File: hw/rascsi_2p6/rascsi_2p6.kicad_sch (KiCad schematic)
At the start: 88 parts, among them IC1 SN74F245DWR, IC2 SN74F245DWR, IC3 SN74F245DWR, IC4 SN74F245DWR, J1 Raspberry_Pi_2_3, J2 DNP, J4 I2C Pinout, J5 DNP, J6 CONNFLY DB-25, X1 Mac, X2 Dogcow, X3 Mac, X4 Dogcow, X5 Dogcow, X6 Dogcow, X7 Pi, X8 Pi

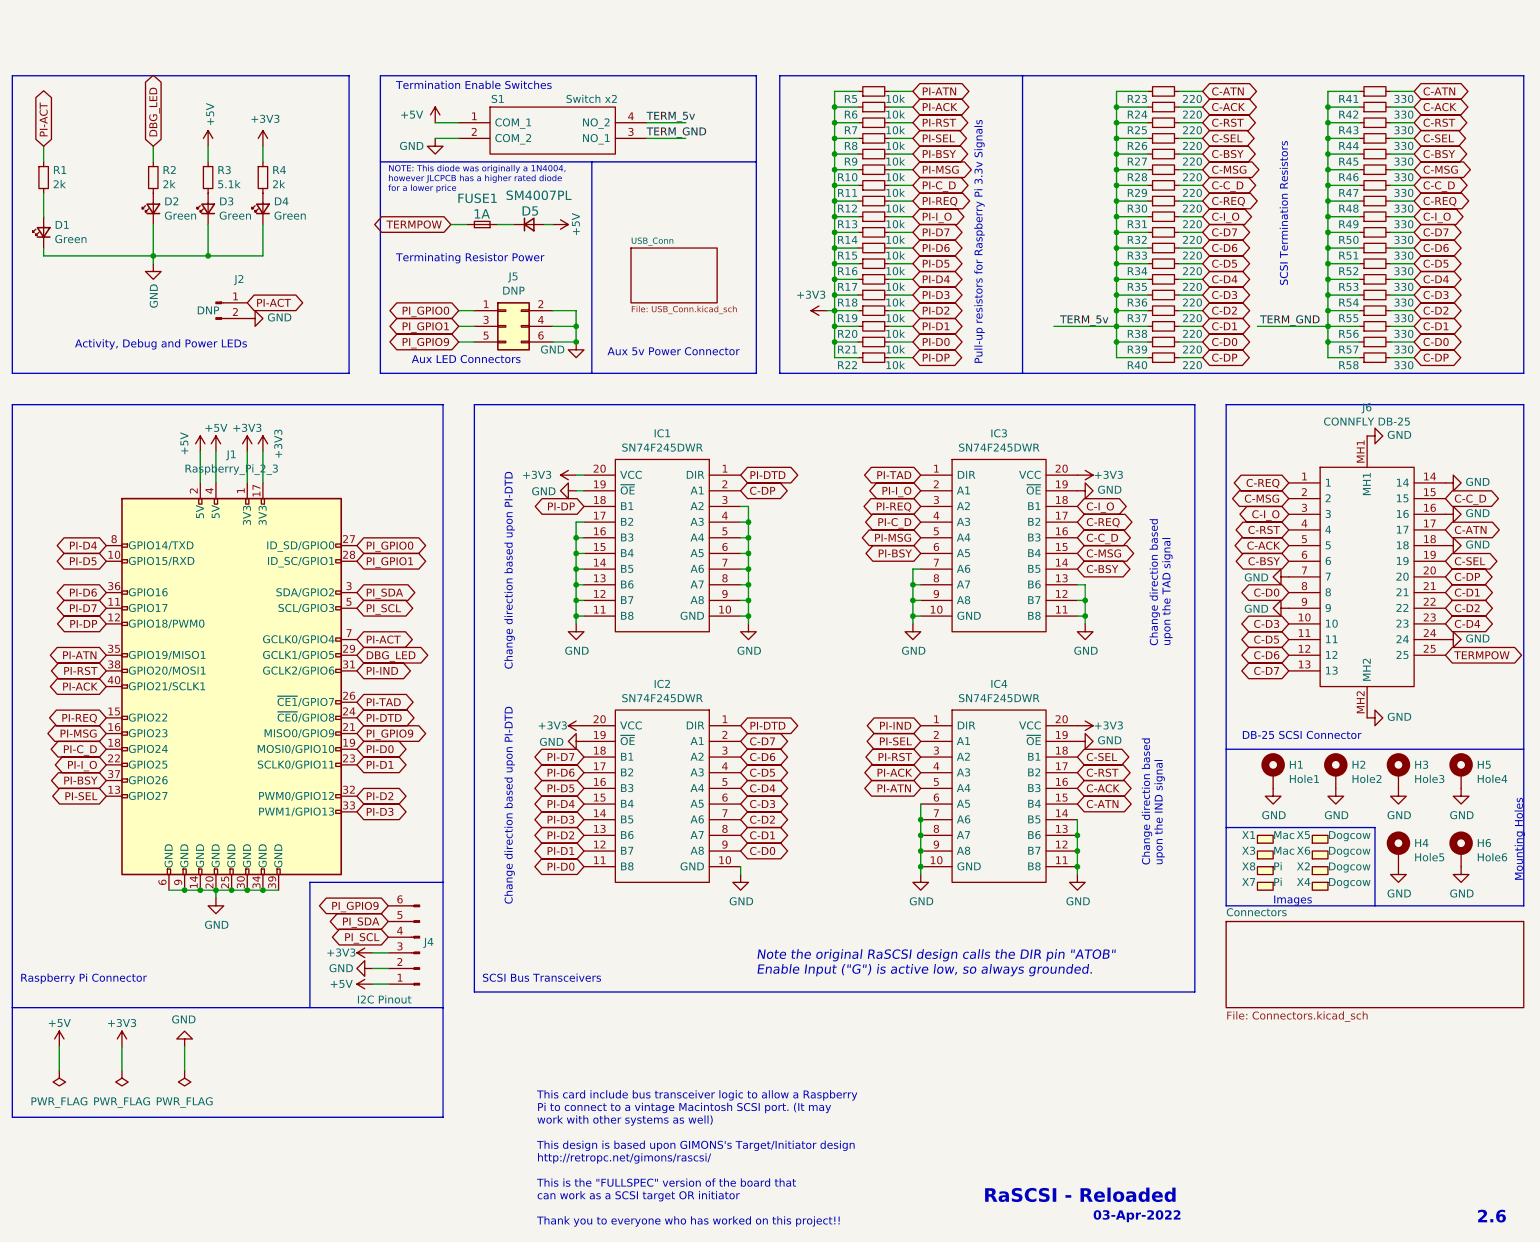
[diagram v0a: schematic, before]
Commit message: Updated with 74LVT245 - as ordered
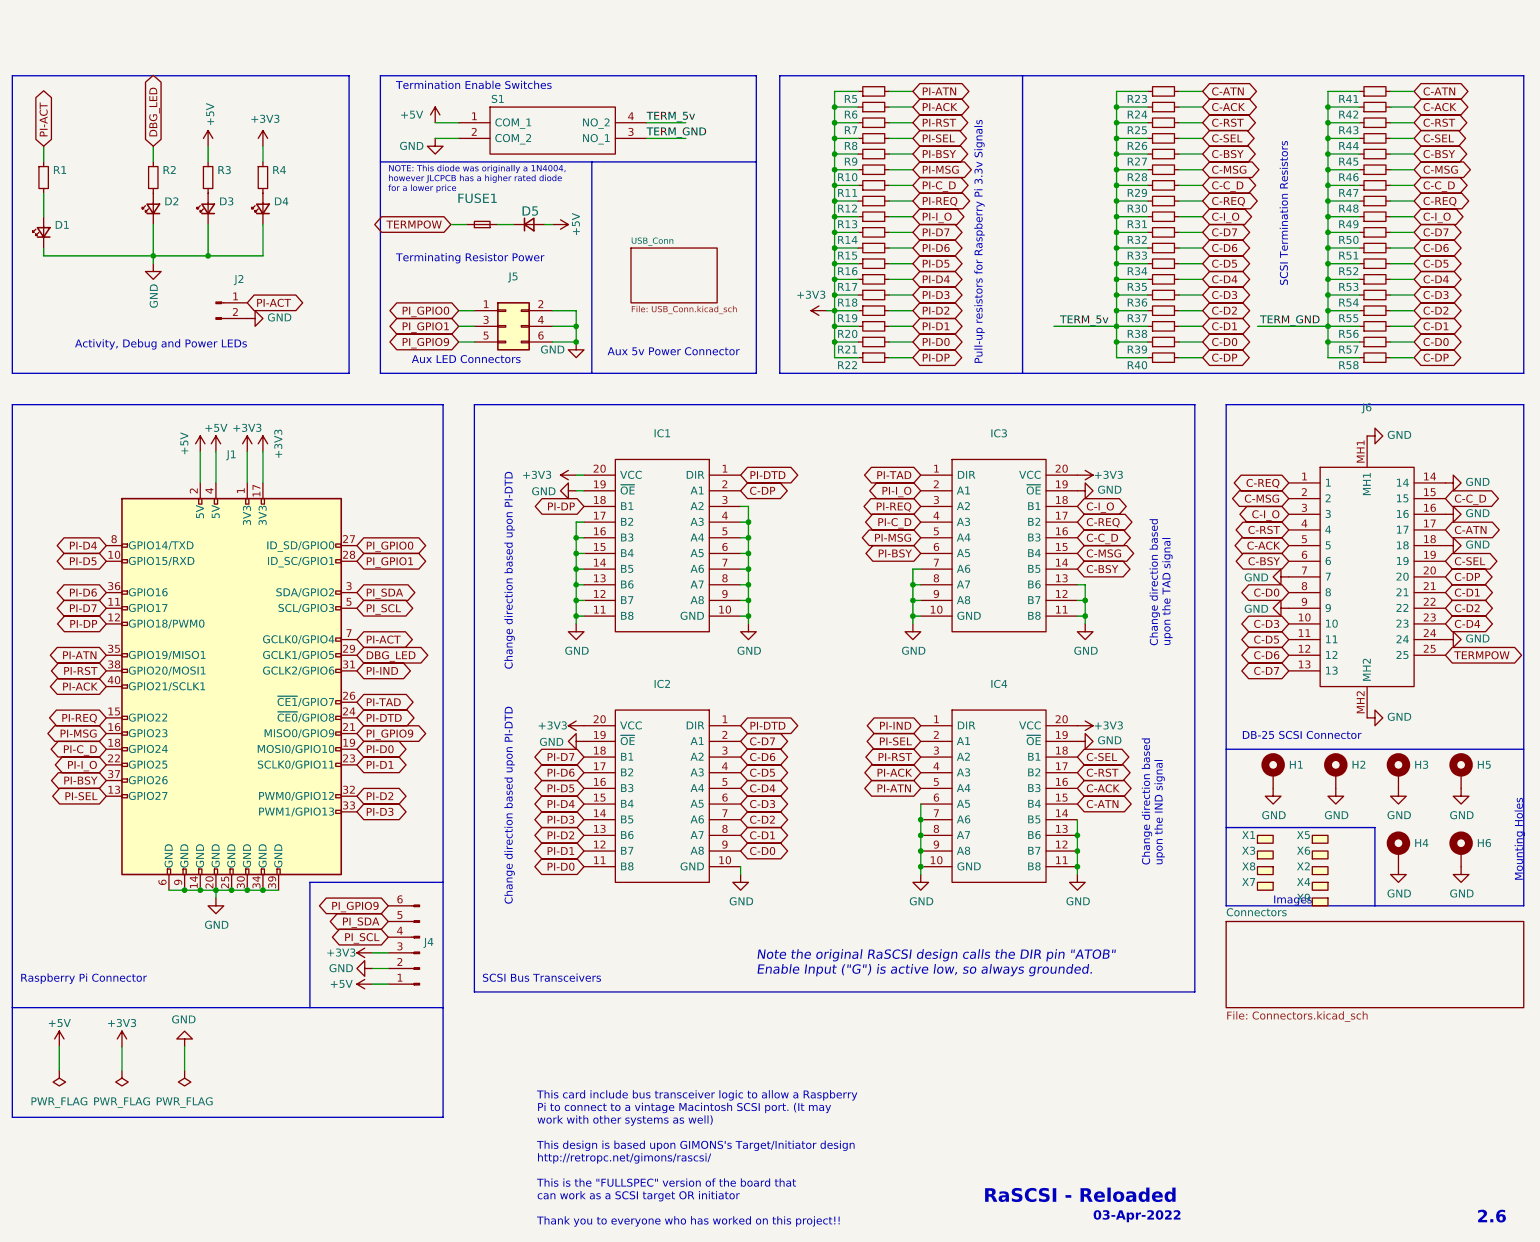
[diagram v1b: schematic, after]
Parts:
- added X9: (no value), symbol SamacSys_Parts:Logo
- D1, D2, D3, D4: value Green -> (none); footprint LED_SMD:LED_0805_2012Metric -> (none)
- D5: value SM4007PL -> (none); footprint Diode_SMD:D_SOD-123F -> (none)
- FUSE1: value 1A -> (none); footprint Fuse:Fuse_1206_3216Metric -> (none)
- H1: value Hole1 -> (none); footprint MountingHole:MountingHole_2.7mm_M2.5_Pad_Via -> (none)
- H2: value Hole2 -> (none); footprint MountingHole:MountingHole_2.7mm_M2.5_Pad_Via -> (none)
- H3: value Hole3 -> (none); footprint MountingHole:MountingHole_2.7mm_M2.5_Pad_Via -> (none)
- H4: value Hole5 -> (none); footprint MountingHole:MountingHole_2.7mm_M2.5_Pad_Via -> (none)
- H5: value Hole4 -> (none); footprint MountingHole:MountingHole_2.7mm_M2.5_Pad_Via -> (none)
- H6: value Hole6 -> (none); footprint MountingHole:MountingHole_2.7mm_M2.5_Pad_Via -> (none)
- IC1, IC2, IC3, IC4: value SN74F245DWR -> (none); footprint SamacSys_Parts:SOIC127P1030X265-20N -> (none); LCSC C7165 -> C74214; Manufacturer_Part_Number SN74F245DWR -> SN74LVT245
- J1: value Raspberry_Pi_2_3 -> (none); footprint Connector_PinSocket_2.54mm:PinSocket_2x20_P2.54mm_Vertical -> (none)
- J2: value DNP -> (none); footprint Connector_PinHeader_2.54mm:PinHeader_1x02_P2.54mm_Horizontal -> (none)
- J4: value I2C Pinout -> (none); footprint Connector_PinSocket_2.54mm:PinSocket_1x06_P2.54mm_Vertical -> (none)
- J5: value DNP -> (none); footprint Connector_PinHeader_2.54mm:PinHeader_2x03_P2.54mm_Vertical -> (none)
- J6: value CONNFLY DB-25 -> (none); footprint SamacSys_Parts:L717SDB25PA4CH4F -> (none)
- R1, R2, R4: value 2k -> (none); footprint Resistor_SMD:R_0402_1005Metric -> (none)
- R10, R11, R12, R13, R14, R15, R16, R17, R18, R19, R20, R21, R22, R5, R6, R7, R8, R9: value 10k -> (none); footprint Resistor_SMD:R_0402_1005Metric -> (none)
- R23, R24, R25, R26, R27, R28, R29, R30, R31, R32, R33, R34, R35, R36, R37, R38, R39, R40: value 220 -> (none); footprint Resistor_SMD:R_0805_2012Metric -> (none)
- R3: value 5.1k -> (none); footprint Resistor_SMD:R_0402_1005Metric -> (none)
- R41, R42, R43, R44, R45, R46, R47, R48, R49, R50, R51, R52, R53, R54, R55, R56, R57, R58: value 330 -> (none); footprint Resistor_SMD:R_0805_2012Metric -> (none)
- S1: value Switch x2 -> (none); footprint rascsi_din:SOIC127P812X230-4N -> (none)
- X1, X3: value Mac -> (none); footprint SamacSys_Parts:mac_happy_small -> (none)
- X2, X4, X5, X6: value Dogcow -> (none); footprint SamacSys_Parts:dogcow -> (none)
- X7: value Pi -> (none); footprint SamacSys_Parts:pi_logo -> (none)
- X8: value Pi -> (none); footprint SamacSys_Parts:scsi_logo -> (none)
